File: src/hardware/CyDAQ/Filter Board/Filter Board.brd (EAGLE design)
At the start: 160.9 x 110.9 mm, 212 parts, among them J1 DCJ0202, J10 Vout_HEADER, J11 5V0_SENSOR, J12 3V3_SENSOR, J13 1V8_SENSOR, J14 BRKOUT_JD, J15 BRKOUT_JC, J16 BRKOUT_JB, J17 BRKOUT_JF, J18 5V0_CONN, J19 3V3_CONN, J2 ZYBO_JF, J20 1V8_CONN, J21 BRKOUT_JD, J3 ZYBO_JE, J4 ZYBO_JD, J5 ZYBO_JC, J6 ZYBO_JB, J7 A_XADC, J8 SJ1-3523N, J9 Vin_HEADER, U1 TPS54531DDARDDA8_3P1X2P4-L, U10 CD74HCT4051, U11 CD74HCT4051, U12 OPA4197, U13 OPA4197, U14 OPA4197, U15 OPA4197, U16 OPA4197, U17 CD74HCT4053, U18 CD74HCT4051, U19 OPA2197, U2 VS-50WQ04FNPBFDPAK-L, U3 TPS56339, U4 TPS56339, U5 LM43601PWPR, U6 X9258_A, U7 X925_B, U8 X9258_C, U9 X9258_D

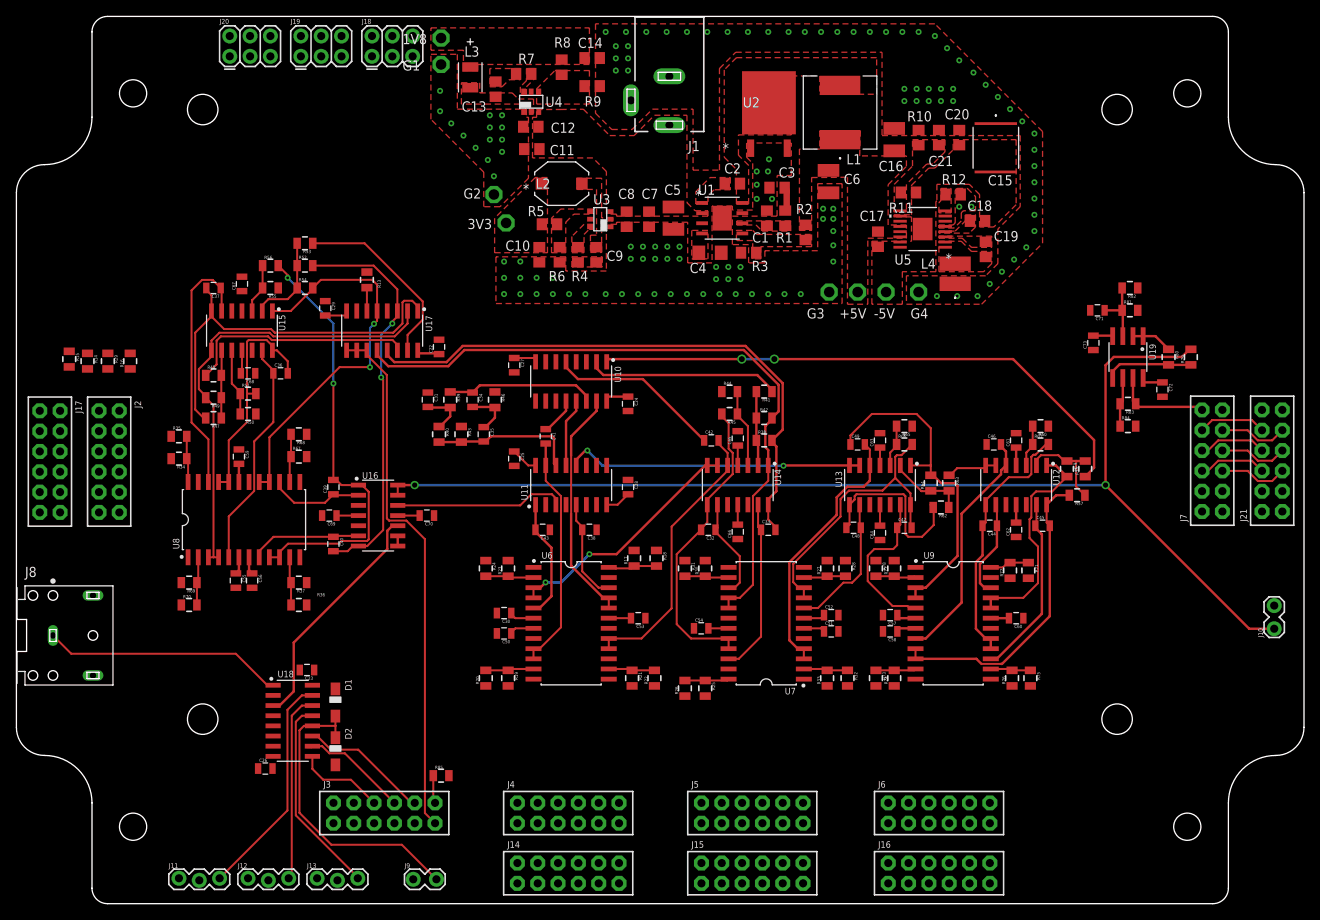
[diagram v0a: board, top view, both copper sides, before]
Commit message: Finished most routing. Need to do -5v rail
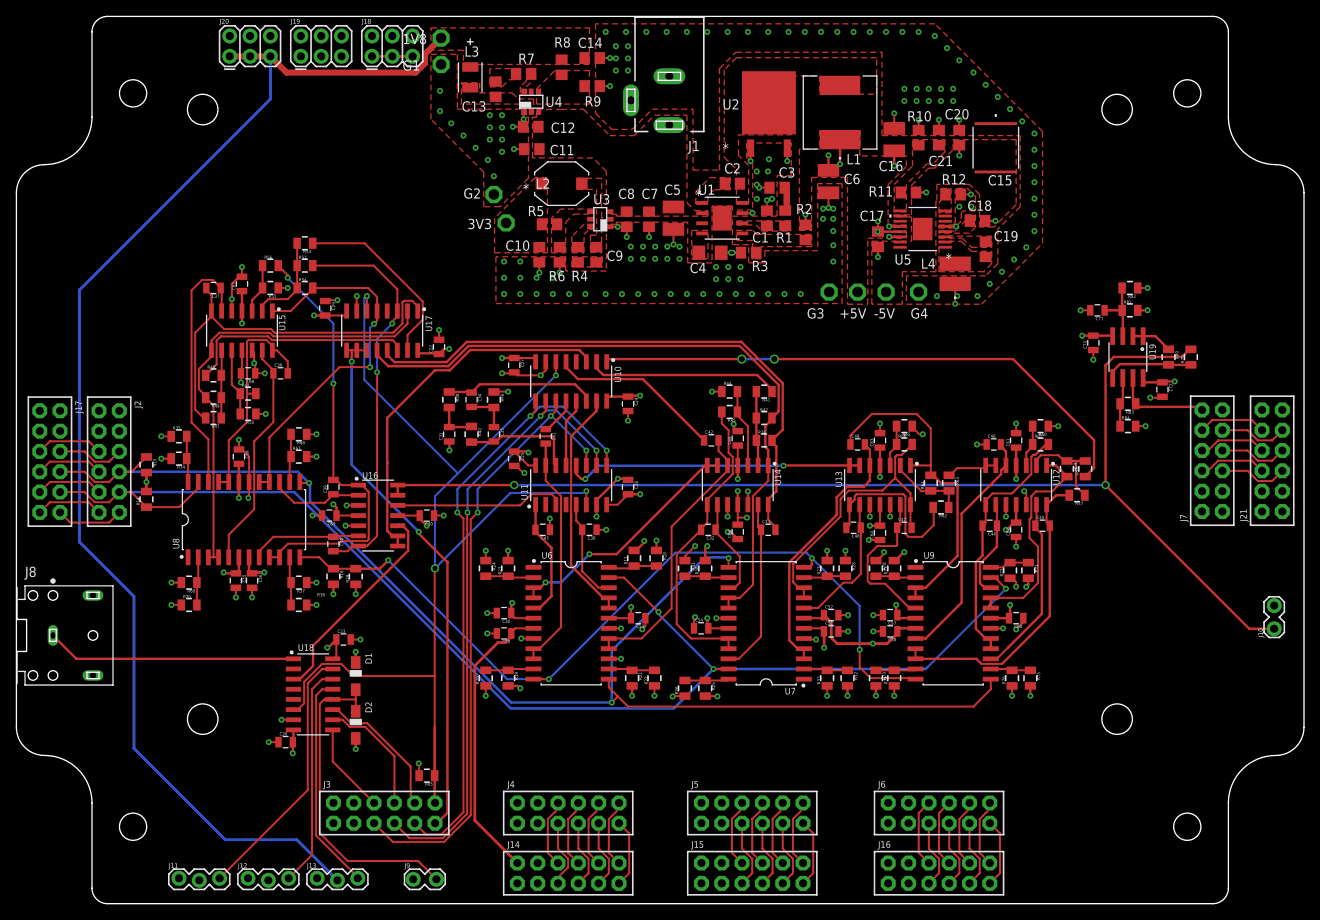
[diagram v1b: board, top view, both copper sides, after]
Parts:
- removed R13: 100k, Resistors:0805
- removed R43: 1k, Resistors:0805
- R14, R15: value 1.5k -> 4.7k
- moved R29 41.1 mm to (42.4, 40.9), turned to 90 degrees
- moved R16 37.0 mm to (39.6, 40.9), turned to 270 degrees
- moved R14 18.8 mm to (16.3, 50.5), turned to 90 degrees
- moved R15 16.4 mm to (16.3, 54.9)
- moved C23 5.95 mm to (40.9, 33.0), turned to 0 degrees
- moved C31 5.08 mm to (54.1, 58.7), turned to 90 degrees
- moved C26 4.17 mm to (33.7, 20.2)
- moved U18 4.17 mm to (37.1, 26.2)
- moved D1 4.17 mm to (42.4, 28.4)
- moved D2 4.17 mm to (42.4, 22.4)
- moved R40 4.06 mm to (56.9, 58.7)
- moved R85 1.78 mm to (51.3, 16.0), turned to 180 degrees
- moved C35 1.27 mm to (59.7, 58.7)
- moved R45 0.25 mm to (89.2, 61.5)
- moved C34 0.13 mm to (56.9, 63.0)
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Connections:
- net 1V8 renamed +1V8
- removed net 3V3: 3V3.TP, C10.1, C50.1, C52.1, C56.1, C58.1, J12.2, J14.1, J14.2, J15.1, J15.2, J16.1, J16.2, J17.1, J17.2, J21.1, J21.2, L2.1, R5.2, U6.7, U7.7, U8.7, U9.7
- removed net 5V0: C16.1, C17.1, C22.1, C23.1, C24.1, C25.1, C30.1, C51.1, C55.1, C57.1, C6.1, C61.1, C63.1, C65.1, C67.1, C69.1, C72.1, D1.1, G3.TP, J11.2, J18.1, J18.3, J18.5, L1.1, R14.2, R15.2, R16.2, R17.2, R19.2, R2.2, R21.2, R23.2, R25.2, R27.2, R30.2, R32.2, R34.2, R36.2, R67.2, R69.2, R71.2, R73.2, R75.2, R77.2, R81.2, U10.16, U11.16, U12.4, U13.4, U14.4, U15.4, U16.4, U17.16, U18.16, U19.8, U5.12, U5.13, U5.14, U6.6, U7.6, U8.6, U9.6
- new net +5V0: C16.1, C17.1, C22.1, C23.1, C24.1, C25.1, C30.1, C51.1, C55.1, C57.1, C6.1, C61.1, C63.1, C65.1, C67.1, C69.1, C72.1, D1.1, G3.TP, J11.2, J18.1, J18.3, J18.5, L1.1, R16.2, R17.2, R19.2, R2.2, R21.2, R23.2, R25.2, R27.2, R30.2, R32.2, R34.2, R36.2, R67.2, R69.2, R71.2, R73.2, R75.2, R77.2, R81.2, U10.16, U11.16, U12.4, U13.4, U14.4, U15.4, U16.4, U17.16, U18.16, U19.8, U5.12, U5.13, U5.14, U6.6, U7.6, U8.6, U9.6
- net !SYSTEM_EN: no longer R13.2
- net +3V3: now also 3V3.TP, C10.1, C50.1, C52.1, C56.1, C58.1, J12.2, J14.1, J14.2, J15.1, J15.2, J16.1, J16.2, J17.1, J17.2, J21.1, J21.2, L2.1, R14.2, R15.2, R5.2, U6.7, U7.7, U8.7, U9.7
- net GND: no longer R13.1, R43.1
- net NOTCH_OUT: no longer R43.2
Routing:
- net +3V3: track 0.00 -> 452.1 mm, vias 0 -> 3
- net SCL: track 0.00 -> 171.4 mm, vias 0 -> 3
- net GND: track 0.00 -> 171.0 mm, vias 126 -> 236
- net SDA: track 0.00 -> 168.9 mm, vias 0 -> 3
- net +1V8: track 0.00 -> 161.2 mm
- net !SYSTEM_EN: track 6.42 -> 143.4 mm, vias 0 -> 4
- net +5V0: track 0.00 -> 107.1 mm, vias 0 -> 41
- net !WP: track 0.00 -> 105.6 mm, vias 0 -> 4
- net FILT_SELECT0: track 0.00 -> 78.7 mm, vias 0 -> 3
- net FILT_SELECT1: track 0.00 -> 78.0 mm, vias 0 -> 3
- net FILT_SELECT2: track 0.00 -> 77.7 mm, vias 0 -> 3
- net VIN_BUFFERED: track 1.27 -> 46.3 mm
- net 5V0: track 33.7 -> 0.00 mm
- net -5V0: track 35.0 -> 65.3 mm, vias 0 -> 20
- net 3V3: track 10.5 -> 0.00 mm
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- added copper zone on layer 1, net +3V3
- added copper zone on layer 1, net +5V0
- added copper zone on layer 15, net +5V0
- removed copper zone on layer 1, net 3V3
- removed copper zone on layer 1, net 5V0

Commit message: Fixed PMOD location
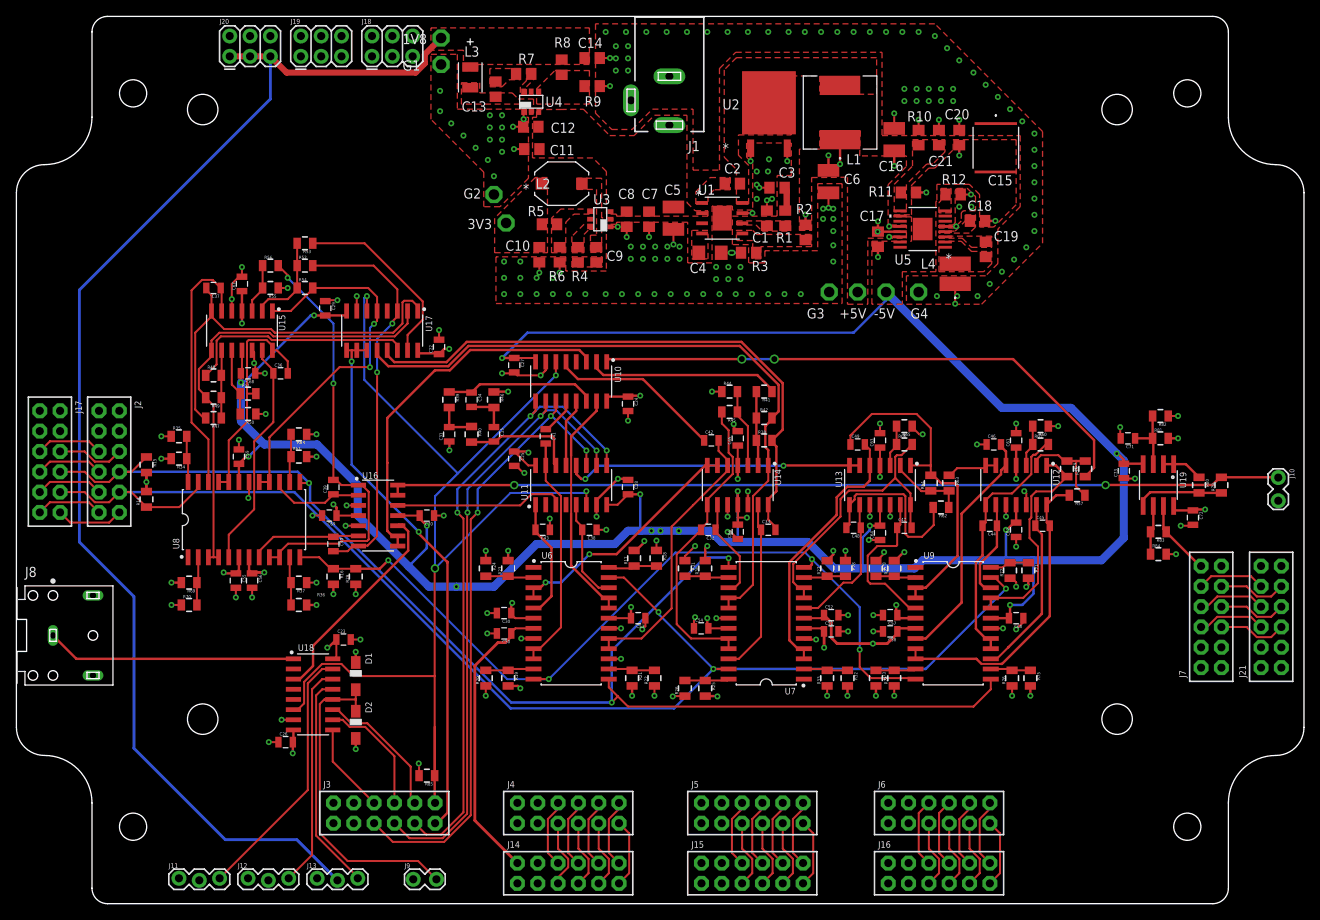
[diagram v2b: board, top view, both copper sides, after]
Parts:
- moved J21 19.5 mm to (158.1, 29.5)
- moved J7 19.5 mm to (150.6, 29.5)
- moved J10 18.5 mm to (157.7, 53.1), turned to 270 degrees
- moved C71 16.4 mm to (138.9, 58.2)
- moved R81 16.4 mm to (143.0, 58.2)
- moved C72 16.4 mm to (147.1, 48.3)
- moved C73 16.4 mm to (138.4, 54.1)
- moved R82 16.4 mm to (143.0, 61.0)
- moved R83 16.4 mm to (142.7, 46.5)
- moved R79 16.4 mm to (150.6, 52.3)
- moved R80 16.4 mm to (147.8, 52.3)
- moved R84 16.4 mm to (142.7, 43.7)
- moved U19 16.4 mm to (142.7, 52.3)
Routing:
- net -5V0: track 65.3 -> 404.6 mm, vias 20 -> 24
- net FILTER_OUT_BUFF: track 144.7 -> 111.8 mm
- net +3V3: track 452.1 -> 432.5 mm
- net +5V0: track 107.1 -> 102.4 mm
- net GND: track 171.0 -> 167.0 mm
- net N$73: track 12.0 -> 9.52 mm

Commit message: Finished routing and made mechanical adjustments
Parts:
- added J22: ZYBO_Power, SparkFun-Connectors:1X02_LOCK
- moved R53 6.51 mm to (41.1, 78.5), turned to 90 degrees
- moved +5V 3.56 mm to (105.2, 76.5)
- moved G3 3.56 mm to (101.6, 76.5)
- moved J10 3.31 mm to (158.0, 56.4)
- moved R52 2.62 mm to (38.4, 78.5), turned to 270 degrees
- moved R54 1.61 mm to (35.6, 78.5), turned to 270 degrees
- moved C26 0.76 mm to (33.7, 19.4)
- moved R50 0.76 mm to (29.0, 60.5)
- moved R51 0.76 mm to (29.0, 63.0)
- moved R71 0.76 mm to (127.3, 41.7)
- moved R72 0.76 mm to (125.0, 41.7)
- moved R60 0.72 mm to (128.5, 60.2)
- moved C46 0.72 mm to (121.7, 57.9)
- moved R61 0.72 mm to (128.5, 57.9)
- moved C49 0.57 mm to (104.6, 57.7)
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- renumbered U2 to D3
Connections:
- new net +5V: J22.2
- net +5V0: now also +5V.TP; no longer G3.TP
- net GND: now also G3.TP, J22.1; no longer +5V.TP
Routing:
- net HP/LP2_IN3: track 24.3 -> 17.7 mm
- net !SYSTEM_EN: track 143.4 -> 137.0 mm
- net GND: track 167.0 -> 163.6 mm, vias 236 -> 234
- net N$38: track 11.7 -> 15.0 mm
- net -5V0: track 404.6 -> 401.4 mm
- net +3V3: track 432.5 -> 435.3 mm
- net LP2_OUT3: track 50.0 -> 47.4 mm
- net N$58: track 27.9 -> 30.0 mm
- net +5V0: track 102.4 -> 100.5 mm, vias 41 -> 42
- net FILTER_OUT_BUFF: track 111.8 -> 113.4 mm
- net VIN_BUFFERED: track 46.3 -> 45.0 mm
- net HP2_OUT3: track 47.0 -> 48.3 mm
- net N$41: track 55.1 -> 53.8 mm
- net N$26: track 9.99 -> 8.81 mm
- net !HP!/LP_TOGGLE: track 68.1 -> 66.9 mm
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- added copper zone on layer 15, net KEEPOUT
- added copper zone on layer 2, net KEEPOUT
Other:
- outline, holes or cut-outs redrawn
- board text added: "+"
- board text added: "+5.0V"
- board text added: "-"
- board text added: "1"
- board text added: "1.2V"
- board text added: "1.8V Sensor"
- board text added: "3.3V"
- board text added: "3.3V Sensor"
- board text added: "5.0V"
- board text added: "5.0V Sensor"
- board text added: "7"
- board text added: "GND"
- board text added: "PWR"
- board text added: "Vin"
- board text removed: "Set ref plane pullback"

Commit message: Added LED and fixed mounting holes
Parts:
- added D4: GREEN, SparkFun-LED:LED-1206
- added R13: 470, rcl:R0805
- C15: device CGA9N3X7R1:CAP_5750-L -> Filter Board:CGA9N3X7R1_CAP_5750
- L1: value IHLP3232DZER4R7M11 -> IHLP-3232DZ_IHLP3232DZER4R7M11; device IHLP-3232DZ:IND_IHLP-3232DZ -> Filter Board:IHLP-3232DZ_IND_IHLP-3232DZ
- L4: device IFSC-1515A:IND_IFSC_1515AH-L -> Filter Board:IFSC-1515A_IND_IFSC_1515AH
- moved L4 1.27 mm to (117.3, 77.5)
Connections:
- new net N$60: D4.C, R13.2
- net +5V0: now also D4.A
- net GND: now also R13.1
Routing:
- net GND: track 163.6 -> 132.1 mm, vias 234 -> 211
- net +5V0: track 100.5 -> 90.4 mm, vias 42 -> 36
- net -5V0: track 401.4 -> 396.3 mm, vias 24 -> 20
- net N$60: track 0.00 -> 3.28 mm
